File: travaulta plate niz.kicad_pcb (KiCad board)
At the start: 4 copper layers, 209.7 x 76.4 mm, 54 parts

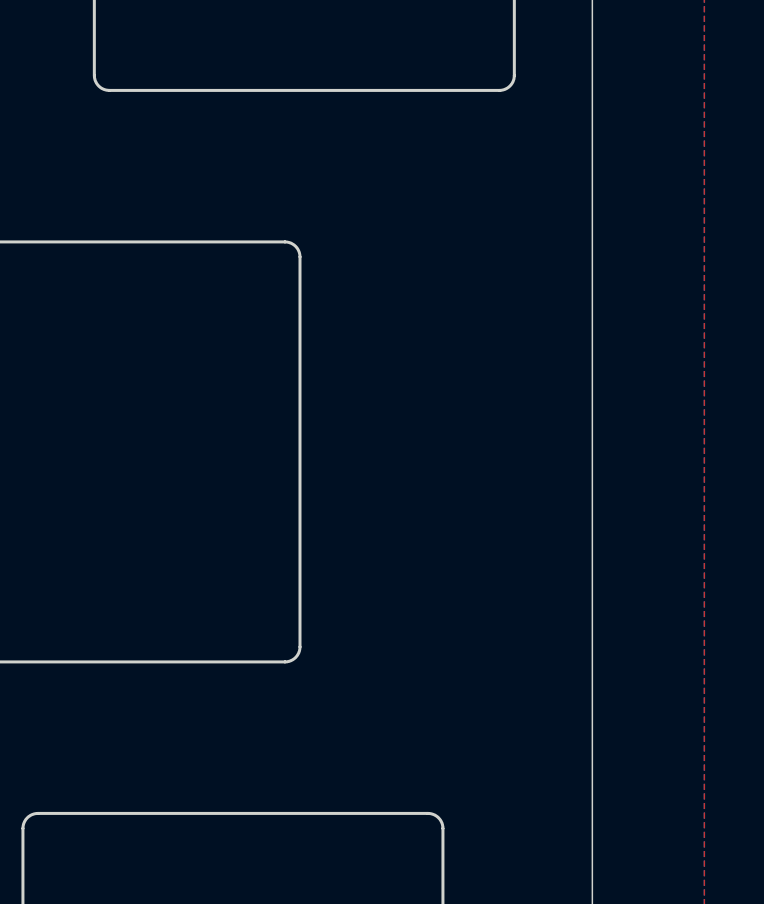
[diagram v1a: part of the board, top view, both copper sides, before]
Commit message: plate cutouts
needs plate edge cut
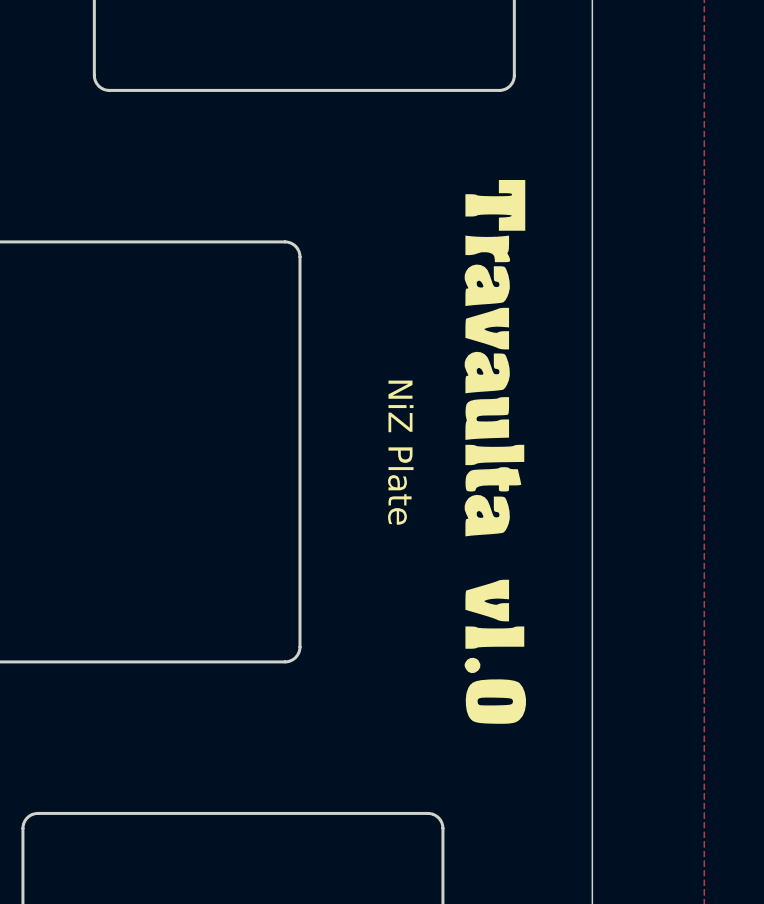
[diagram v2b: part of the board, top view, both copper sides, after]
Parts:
- added G***: LOGO, LOGO, F.Cu at (250.8, 76.2)
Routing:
- removed copper zone on In1.Cu, net GND
- removed copper zone on In2.Cu, net GND
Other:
- copper layers 4 -> 2
- board text added: "NiZ Plate"

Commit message: first draft plates complete
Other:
- board size 209.7 x 76.4 mm -> 210.7 x 77.4 mm

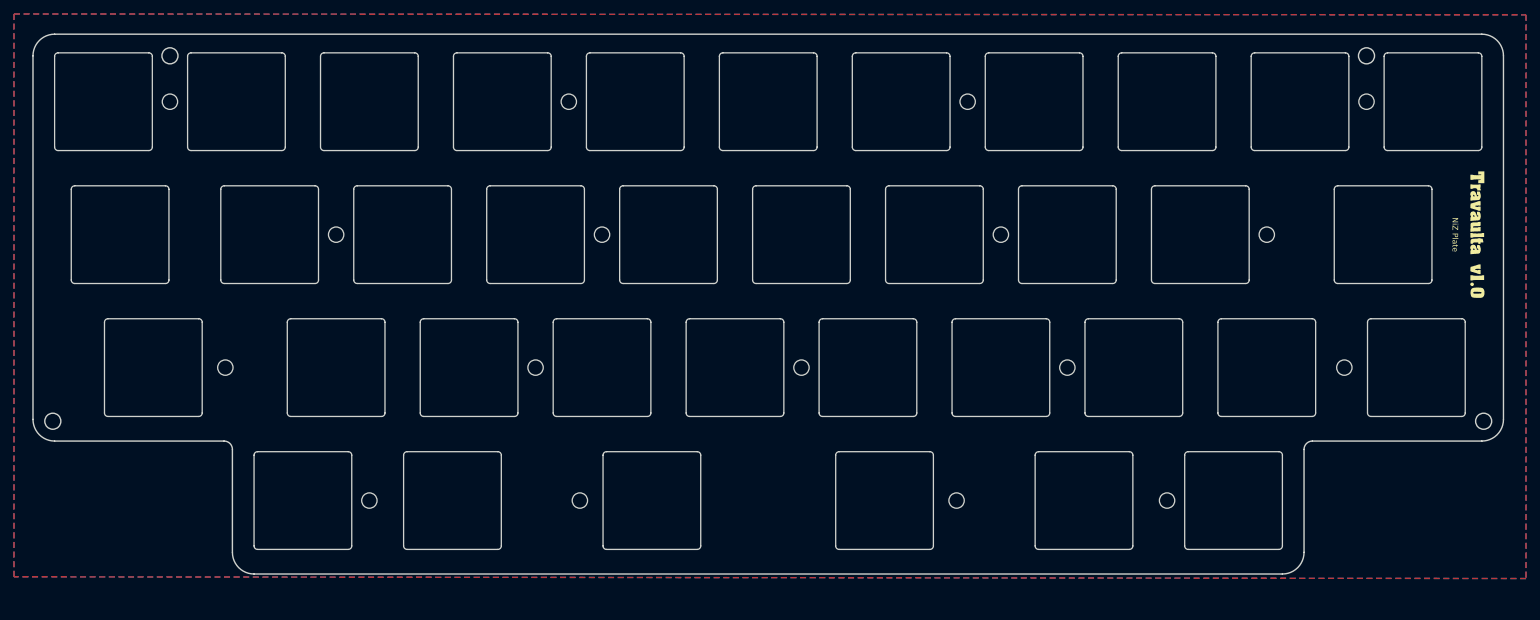
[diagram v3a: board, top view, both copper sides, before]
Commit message: edited preliminary firmware, small routing cleanups
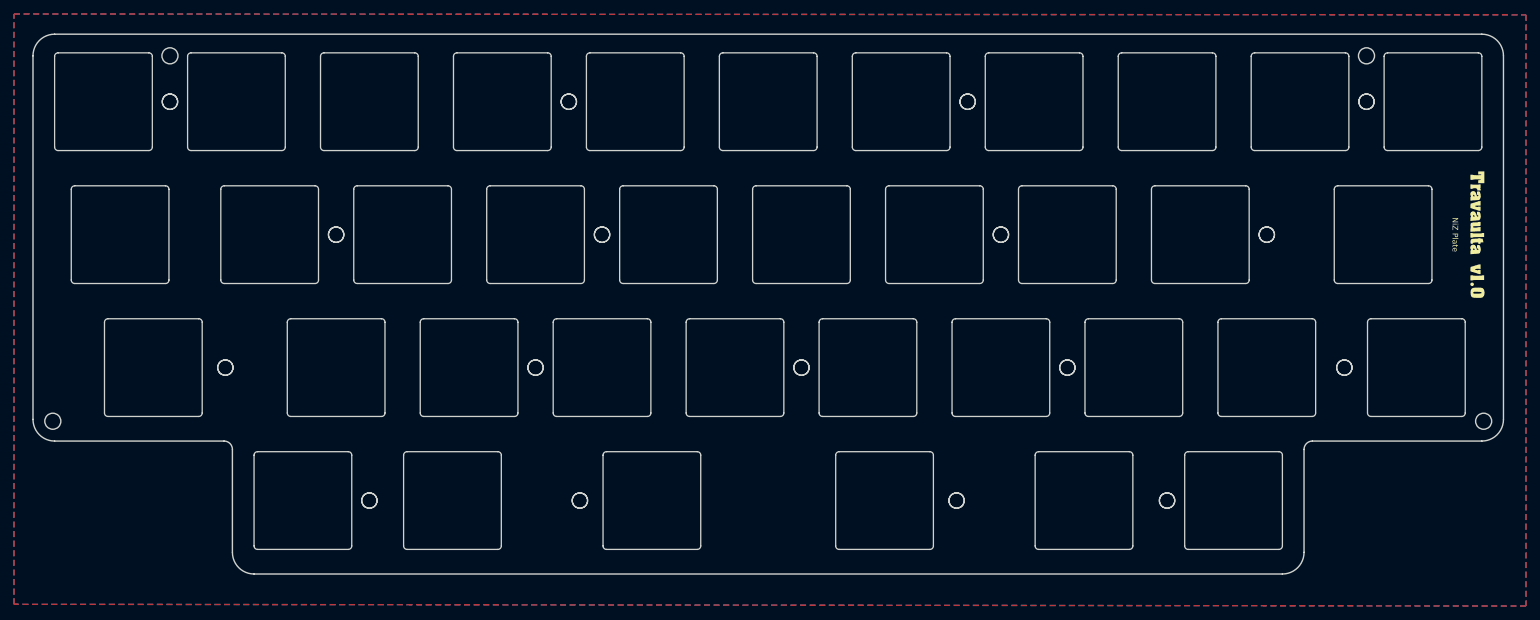
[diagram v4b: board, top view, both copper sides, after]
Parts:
- added H1: MountingHole, cipulot_parts:HOLE_M2, F.Cu at (63.5, 57.1)
- added H10: MountingHole, cipulot_parts:HOLE_M2, F.Cu at (115.9, 95.2)
- added H11: MountingHole, cipulot_parts:HOLE_M2, F.Cu at (154.0, 95.2)
- added H12: MountingHole, cipulot_parts:HOLE_M2, F.Cu at (192.1, 95.2)
- added H13: MountingHole, cipulot_parts:HOLE_M2, F.Cu at (231.8, 95.2)
- added H14: MountingHole, cipulot_parts:HOLE_M2, F.Cu at (92.1, 114.3)
- added H15: MountingHole, cipulot_parts:HOLE_M2, F.Cu at (122.2, 114.3)
- added H16: MountingHole, cipulot_parts:HOLE_M2, F.Cu at (176.2, 114.3)
- added H17: MountingHole, cipulot_parts:HOLE_M2, F.Cu at (206.4, 114.3)
- added H2: MountingHole, cipulot_parts:HOLE_M2, F.Cu at (120.7, 57.1)
- added H3: MountingHole, cipulot_parts:HOLE_M2, F.Cu at (177.8, 57.1)
- added H4: MountingHole, cipulot_parts:HOLE_M2, F.Cu at (234.9, 57.1)
- added H5: MountingHole, cipulot_parts:HOLE_M2, F.Cu at (87.3, 76.2)
- added H6: MountingHole, cipulot_parts:HOLE_M2, F.Cu at (125.4, 76.2)
- added H7: MountingHole, cipulot_parts:HOLE_M2, F.Cu at (182.6, 76.2)
- added H8: MountingHole, cipulot_parts:HOLE_M2, F.Cu at (220.7, 76.2)
- added H9: MountingHole, cipulot_parts:HOLE_M2, F.Cu at (71.4, 95.2)
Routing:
- added copper zone on B.Cu, net (none)
- added copper zone on F.Cu, net (none)
- removed copper zone on B.Cu, net GND
- removed copper zone on F.Cu, net GND

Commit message: fresh gerbers
deleted old plate gerbers, need new export
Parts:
- removed the ? at (231.8, 95.2)
- removed H15, H16, H9: MountingHole, cipulot_parts:HOLE_M2
- moved ? 0.79 mm to (175.4, 114.3)
- moved ? 0.79 mm to (70.6, 95.2)
- moved ? 0.79 mm to (123.0, 114.3)
- moved H13 0.79 mm to (232.6, 95.2)
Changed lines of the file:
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@@
   )
   (footprint "cipulot_parts:HOLE_M2" (layer "F.Cu")
-    (at 231.775 95.25)
+    (at 232.56875 95.25)
     (property "Sheetfile" "travaulta plate niz.kicad_sch")
     (property "Sheetname" "")
@@
   )
   (footprint "" (layer "F.Cu")
-    (at 176.2125 114.3)
+    (at 175.41875 114.3)
     (attr board_only)
     (fp_text reference "" (at 0 0) (layer "F.SilkS")
@@
   )
   (footprint "" (layer "F.Cu")
-    (at 71.4375 95.25)
+    (at 70.64375 95.25)
     (attr board_only)
     (fp_text reference "" (at 0 0) (layer "F.SilkS")
@@
     )
   )
-  (footprint "cipulot_parts:HOLE_M2" (layer "F.Cu")
-    (at 176.2125 114.3)
-    (property "Sheetfile" "travaulta plate niz.kicad_sch")
-    (property "Sheetname" "")
-    (property "ki_description" "Mounting Hole without connection")
-    (property "ki_keywords" "mounting hole")
-    (attr through_hole)
-    (fp_text reference "H16" (at 0 -2) (layer "F.SilkS") hide
-        (effects (font (size 0.29972 0.29972) (thickness 0.07493)))
-    )
-    (fp_text value "MountingHole" (at 0 2.2352) (layer "F.SilkS") hide
-        (effects (font (size 0.29972 0.29972) (thickness 0.07493)))
-    )
-    (pad "" np_thru_hole circle (at 0 0) (size 2.2 2.2) (drill 2.2) (layers "F&B.Cu" "*.Mask" "F.SilkS")
-      (clearance 0.5))
-  )
   (footprint "cipulot_parts:plate_cut_ecs_pad_NIZ" (layer "F.Cu")
     (at 163.5125 95.25)
@@
   )
   (footprint "" (layer "F.Cu")
-    (at 122.2375 114.3)
+    (at 123.03125 114.3)
     (attr board_only)
     (fp_text reference "" (at 0 0) (layer "F.SilkS")
@@
       (rotate (xyz 0 0 0))
     )
-  )
-  (footprint "cipulot_parts:HOLE_M2" (layer "F.Cu")
-    (at 122.2375 114.3)
-    (property "Sheetfile" "travaulta plate niz.kicad_sch")
-    (property "Sheetname" "")
-    (property "ki_description" "Mounting Hole without connection")
-    (property "ki_keywords" "mounting hole")
-    (attr through_hole)
-    (fp_text reference "H15" (at 0 -2) (layer "F.SilkS") hide
-        (effects (font (size 0.29972 0.29972) (thickness 0.07493)))
-    )
-    (fp_text value "MountingHole" (at 0 2.2352) (layer "F.SilkS") hide
-        (effects (font (size 0.29972 0.29972) (thickness 0.07493)))
-    )
-    (pad "" np_thru_hole circle (at 0 0) (size 2.2 2.2) (drill 2.2) (layers "F&B.Cu" "*.Mask" "F.SilkS")
-      (clearance 0.5))
   )
   (footprint "" locked (layer "F.Cu")
@@
     )
   )
-  (footprint "" (layer "F.Cu")
-    (at 231.775 95.25)
-    (attr board_only)
-    (fp_text reference "" (at 0 0) (layer "F.SilkS")
-        (effects (font (size 1.27 1.27) (thickness 0.15)))
-    )
-    (fp_text value "" (at 0 0) (layer "F.SilkS")
-        (effects (font (size 1.27 1.27) (thickness 0.15)))
-    )
-    (pad "" np_thru_hole circle (at 0 0) (size 2.2 2.2) (drill 2.2) (layers "*.Cu" "*.Mask" "F.SilkS")
-      (clearance 0.5))
-  )
   (footprint "cipulot_parts:HOLE_M2" (layer "F.Cu")
     (at 153.9875 95.25)
@@
       (clearance 0.5))
   )
-  (footprint "cipulot_parts:HOLE_M2" (layer "F.Cu")
-    (at 71.4375 95.25)
-    (property "Sheetfile" "travaulta plate niz.kicad_sch")
-    (property "Sheetname" "")
-    (property "ki_description" "Mounting Hole without connection")
-    (property "ki_keywords" "mounting hole")
-    (attr through_hole)
-    (fp_text reference "H9" (at 0 -2) (layer "F.SilkS") hide
-        (effects (font (size 0.29972 0.29972) (thickness 0.07493)))
-    )
-    (fp_text value "MountingHole" (at 0 2.2352) (layer "F.SilkS") hide
-        (effects (font (size 0.29972 0.29972) (thickness 0.07493)))
-    )
-    (pad "" np_thru_hole circle (at 0 0) (size 2.2 2.2) (drill 2.2) (layers "F&B.Cu" "*.Mask" "F.SilkS")
-      (clearance 0.5))
-  )

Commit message: pcb clean up, fresh gerbers
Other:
- board text added: "JLCJLCJLCJLC"
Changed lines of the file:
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@@
   (gr_line (start 71.25 105.774999) (end 46.975 105.774999)
     (stroke (width 0.2) (type solid)) (layer "Edge.Cuts"))
+  (gr_text "JLCJLCJLCJLC" (at 249.2375 76.2 -90) (layer "B.SilkS")
+    (effects (font (size 1 1) (thickness 0.15)))
+  )
   (gr_text "NiZ Plate" (at 247.65 76.2 270) (layer "F.SilkS")
     (effects (font (size 0.8 0.8) (thickness 0.15)))
